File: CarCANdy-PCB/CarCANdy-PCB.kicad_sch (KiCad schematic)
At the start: 87 parts, among them J1 8P8C_Shielded, J10 ADC1, J11 ADC1, J12 ADC1, J13 Conn_01x02_Pin, J14 Conn_01x02_Pin, J15 Conn_01x02_Pin, J2 Power, J4 AUART1, J5 JSTVH3, J6 JSTVH3, J7 JSTVH3, J8 AUART1, K3 IM02, K4 IM02, K5 IM02, Q1 AO3400A, Q2 AO3400A, Q3 AO3400A, SW2 JS202011CQN, SW3 JS202011CQN, SW4 JS202011CQN, U1 LTV-357T, U2 ESP32-C3_SUPERMINI_TH, U3 SN65HVD233DR, U4 SN65HVD233DR, U5 SN65HVD233DR, U6 Teensy4.1, U7 LTV-357T, U8 LTV-357T

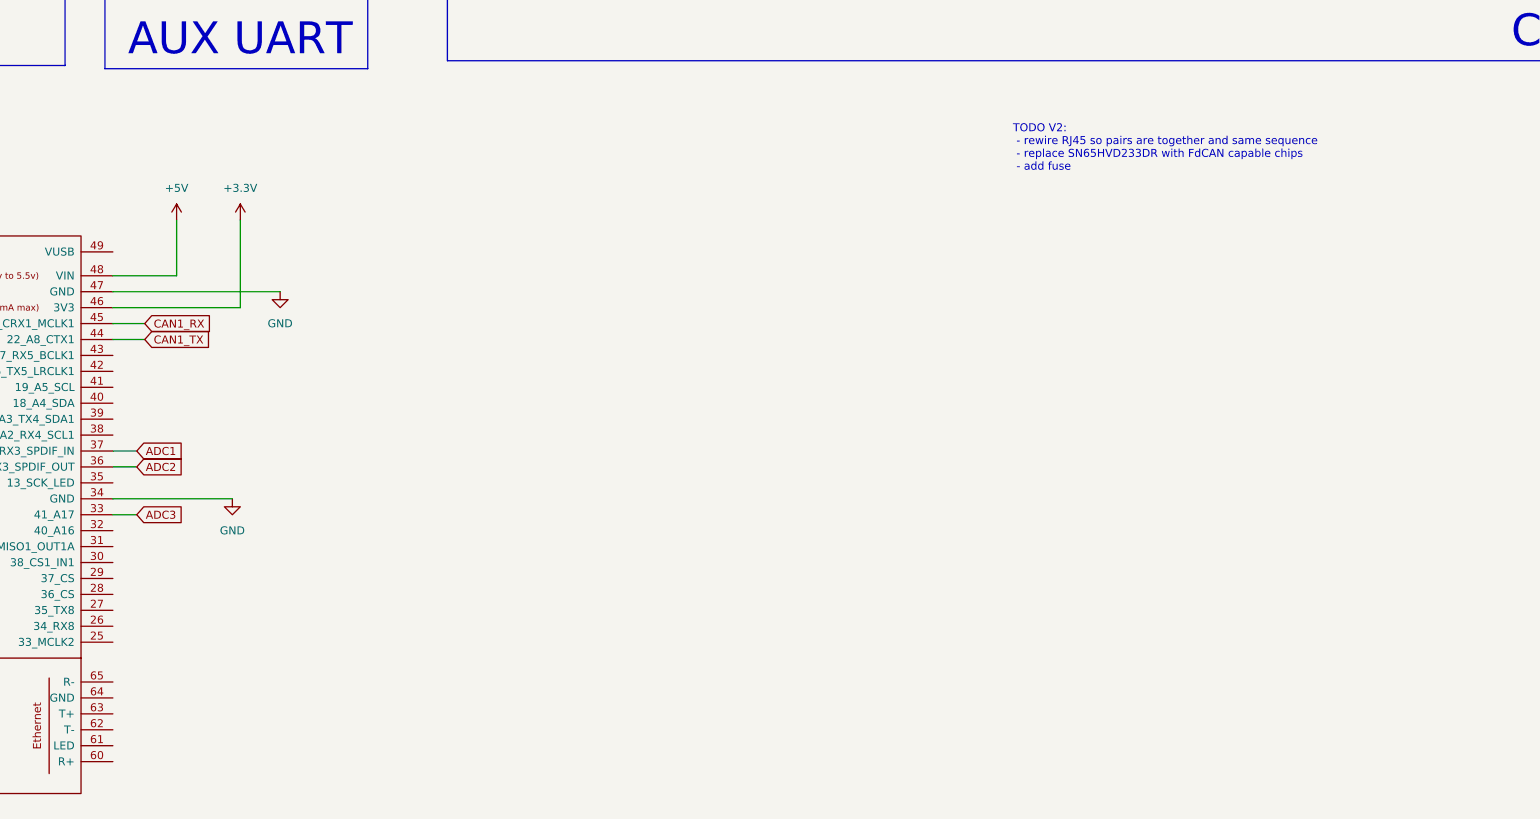
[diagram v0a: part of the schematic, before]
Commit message: simplified CANDB json
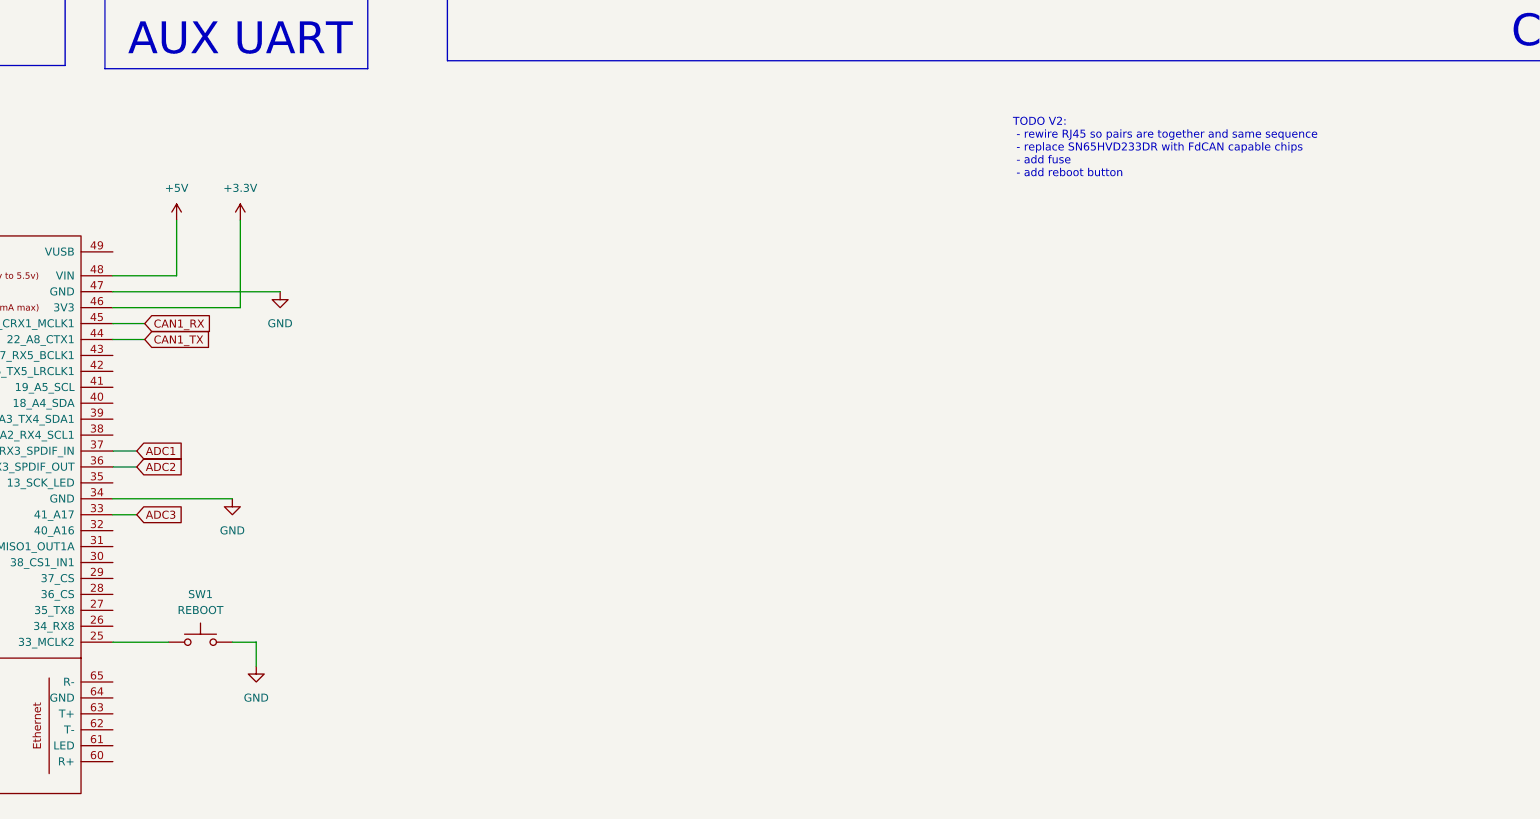
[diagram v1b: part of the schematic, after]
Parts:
- added SW1: REBOOT, Button_Switch_SMD:SW_Push_1P1T_NO_CK_KMR2, symbol Switch:SW_Push
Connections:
- net GND: now also SW1.2
- net at U6.25 (33_MCLK2): now also SW1.1
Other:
- note added: "TODO V2: - rewire RJ45 so pairs are together and same sequence - replace SN65HVD233DR with FdCAN capable chips - add fuse - add reboot button"
- note removed: "TODO V2: - rewire RJ45 so pairs are together and same sequence - replace SN65HVD233DR with FdCAN capable chips - add fuse"
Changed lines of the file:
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@@
 		)
 	)
-	(text "TODO V2: \n - rewire RJ45 so pairs are together and same sequence\n - replace SN65HVD233DR with FdCAN capable chips\n - add fuse"
+	(text "TODO V2: \n - rewire RJ45 so pairs are together and same sequence\n - replace SN65HVD233DR with FdCAN capable chips\n - add fuse\n - add reboot button"
 		(exclude_from_sim no)
 		(at 547.37 163.83 0)
@@
 	(wire
 		(pts
+			(xy 422.91 242.57) (xy 426.72 242.57)
+		)
+		(stroke
+			(width 0)
+			(type default)
+		)
+	)
+	(wire
+		(pts
 			(xy 139.7 214.63) (xy 139.7 207.01)
 		)
@@
 	(wire
 		(pts
+			(xy 403.86 242.57) (xy 412.75 242.57)
+		)
+		(stroke
+			(width 0)
+			(type default)
+		)
+	)
+	(wire
+		(pts
 			(xy 594.36 53.34) (xy 596.9 53.34)
 		)
@@
 	(wire
 		(pts
+			(xy 426.72 242.57) (xy 426.72 246.38)
+		)
+		(stroke
+			(width 0)
+			(type default)
+		)
+	)
+	(wire
+		(pts
 			(xy 344.17 189.23) (xy 347.98 189.23)
 		)
@@
 	(symbol
 		(lib_id "power:GND")
+		(at 426.72 246.38 0)
+		(unit 1)
+		(body_style 1)
+		(exclude_from_sim no)
+		(in_bom yes)
+		(on_board yes)
+		(in_pos_files yes)
+		(dnp no)
+		(fields_autoplaced yes)
+		(property "Reference" "#PWR075"
+			(at 426.72 252.73 0)
+			(hide yes)
+			(show_name no)
+			(do_not_autoplace no)
+			(effects
+				(font
+					(size 1.27 1.27)
+				)
+			)
+		)
+		(property "Value" "GND"
+			(at 426.72 251.46 0)
+			(show_name no)
+			(do_not_autoplace no)
+			(effects
+				(font
+					(size 1.27 1.27)
+				)
+			)
+		)
+		(property "Footprint" ""
+			(at 426.72 246.38 0)
+			(hide yes)
+			(show_name no)
+			(do_not_autoplace no)
+			(effects
+				(font
+					(size 1.27 1.27)
+				)
+			)
+		)
+		(property "Datasheet" ""
+			(at 426.72 246.38 0)
+			(hide yes)
+			(show_name no)
+			(do_not_autoplace no)
+			(effects
+				(font
+					(size 1.27 1.27)
+				)
+			)
+		)
+		(property "Description" "Power symbol creates a global label with name \"GND\" , ground"
+			(at 426.72 246.38 0)
+			(hide yes)
+			(show_name no)
+			(do_not_autoplace no)
+			(effects
+				(font
+					(size 1.27 1.27)
+				)
+			)
+		)
+		(pin "1"
+		)
+		(instances
+			(project "CarCANdy-PCB"
+				(path "/971987f6-db6c-4f58-a887-69a69687dd52"
+					(reference "#PWR075")
+					(unit 1)
+				)
+			)
+		)
+	)
+	(symbol
+		(lib_id "power:GND")
 		(at 50.8 151.13 0)
 		(unit 1)
@@
 					(unit 1)
 				)
+			)
+		)
+	)
+	(symbol
+		(lib_id "Switch:SW_Push")
+		(at 417.83 242.57 0)
+		(unit 1)
+		(body_style 1)
+		(exclude_from_sim no)
+		(in_bom yes)
+		(on_board yes)
+		(in_pos_files yes)
+		(dnp no)
+		(fields_autoplaced yes)
+		(property "Reference" "SW1"
+			(at 417.83 234.95 0)
+			(show_name no)
+			(do_not_autoplace no)
+			(effects
+				(font
+					(size 1.27 1.27)
+				)
+			)
+		)
+		(property "Value" "REBOOT"
+			(at 417.83 237.49 0)
+			(show_name no)
+			(do_not_autoplace no)
+			(effects
+				(font
+					(size 1.27 1.27)
+				)
+			)
+		)
+		(property "Footprint" "Button_Switch_SMD:SW_Push_1P1T_NO_CK_KMR2"
+			(at 417.83 237.49 0)
+			(hide yes)
+			(show_name no)
+			(do_not_autoplace no)
+			(effects
+				(font
+					(size 1.27 1.27)
+				)
+			)
+		)
+		(property "Datasheet" ""
+			(at 417.83 237.49 0)
+			(hide yes)
+			(show_name no)
+			(do_not_autoplace no)
+			(effects
+				(font
+					(size 1.27 1.27)
+				)
+			)
+		)
+		(property "Description" "Push button switch, generic, two pins"
+			(at 417.83 242.57 0)
+			(hide yes)
+			(show_name no)
+			(do_not_autoplace no)
+			(effects
+				(font
+					(size 1.27 1.27)
+				)
+			)
+		)
+		(pin "2"
+		)
+		(pin "1"
+		)
+		(instances
+			(project "CarCANdy-PCB"
+				(path "/971987f6-db6c-4f58-a887-69a69687dd52"
+					(reference "SW1")
+					(unit 1)
+				)

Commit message: bug fixes in PCB
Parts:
- added D15, D16: 1N4148W, Diode_SMD:D_SOD-123, symbol Diode:1N4148W
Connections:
- net +5V: now also D15.2 (A), D16.2 (A); no longer U2.5V, U6.48 (VIN)
- net CAN2_RX: now also U6.2 (0_RX1_CRX2_CS1); no longer U6.3 (1_TX1_CTX2_MISO1)
- net CAN2_TX: now also U6.3 (1_TX1_CTX2_MISO1); no longer U6.2 (0_RX1_CRX2_CS1)
- new net: D15.1 (K), U6.48 (VIN)
- new net: D16.1 (K), U2.5V
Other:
- note added: "Teensy 4.1"
- moved on the sheet: C2, C3, C4, C5, C6, C7, D10, D11, D12, D13, D14, D5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

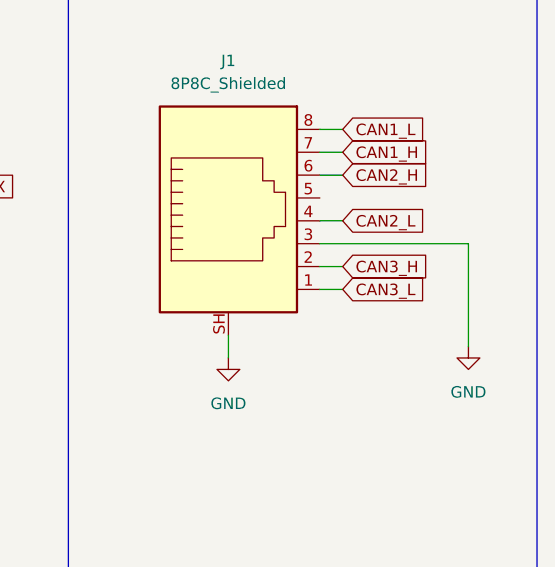
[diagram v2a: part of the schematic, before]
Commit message: added diodes to power rails, rewired RJ45
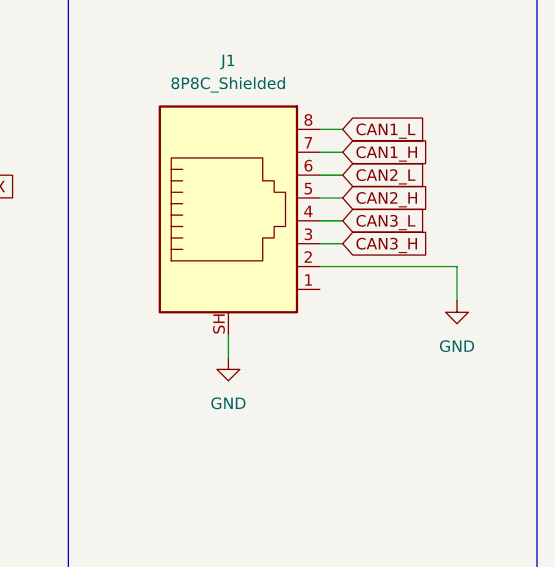
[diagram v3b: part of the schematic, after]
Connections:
- net CAN2_H: now also J1.5; no longer J1.6
- net CAN2_L: now also J1.6; no longer J1.4
- net CAN3_H: now also J1.3; no longer J1.2
- net CAN3_L: now also J1.4; no longer J1.1
- net GND: now also J1.2; no longer J1.3
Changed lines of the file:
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@@
 	(wire
 		(pts
-			(xy 796.29 67.31) (xy 798.83 67.31)
-		)
-		(stroke
-			(width 0)
-			(type default)
-		)
-	)
-	(wire
-		(pts
 			(xy 492.76 66.04) (xy 492.76 68.58)
 		)
@@
 	(wire
 		(pts
-			(xy 796.29 80.01) (xy 798.83 80.01)
-		)
-		(stroke
-			(width 0)
-			(type default)
-		)
-	)
-	(wire
-		(pts
 			(xy 612.14 290.83) (xy 613.41 290.83)
 		)
@@
 	(wire
 		(pts
-			(xy 796.29 77.47) (xy 812.8 77.47)
-		)
-		(stroke
-			(width 0)
-			(type default)
-		)
-	)
-	(wire
-		(pts
 			(xy 631.19 288.29) (xy 631.19 290.83)
 		)
@@
 	(wire
 		(pts
-			(xy 796.29 74.93) (xy 798.83 74.93)
-		)
-		(stroke
-			(width 0)
-			(type default)
-		)
-	)
-	(wire
-		(pts
 			(xy 506.73 270.51) (xy 511.81 270.51)
 		)
@@
 	(wire
 		(pts
-			(xy 565.15 220.98) (xy 565.15 198.12)
+			(xy 811.53 80.01) (xy 811.53 83.82)
 		)
 		(stroke
@@
 	(wire
 		(pts
-			(xy 609.6 86.36) (xy 610.87 86.36)
+			(xy 565.15 220.98) (xy 565.15 198.12)
 		)
 		(stroke
@@
 	(wire
 		(pts
-			(xy 570.23 267.97) (xy 607.06 267.97)
+			(xy 609.6 86.36) (xy 610.87 86.36)
 		)
 		(stroke
@@
 	(wire
 		(pts
-			(xy 172.72 50.8) (xy 176.53 50.8)
+			(xy 570.23 267.97) (xy 607.06 267.97)
 		)
 		(stroke
@@
 	(wire
 		(pts
-			(xy 511.81 290.83) (xy 513.08 290.83)
+			(xy 172.72 50.8) (xy 176.53 50.8)
 		)
 		(stroke
@@
 	(wire
 		(pts
-			(xy 812.8 88.9) (xy 812.8 77.47)
+			(xy 511.81 290.83) (xy 513.08 290.83)
 		)
 		(stroke
@@
 	(wire
 		(pts
+			(xy 796.29 72.39) (xy 798.83 72.39)
+		)
+		(stroke
+			(width 0)
+			(type default)
+		)
+	)
+	(wire
+		(pts
 			(xy 683.26 285.75) (xy 685.8 285.75)
 		)
@@
 	(wire
 		(pts
-			(xy 796.29 82.55) (xy 798.83 82.55)
-		)
-		(stroke
-			(width 0)
-			(type default)
-		)
-	)
-	(wire
-		(pts
-			(xy 796.29 64.77) (xy 798.83 64.77)
-		)
-		(stroke
-			(width 0)
-			(type default)
-		)
-	)
-	(wire
-		(pts
 			(xy 511.81 302.26) (xy 511.81 295.91)
 		)
@@
 	(wire
 		(pts
+			(xy 796.29 64.77) (xy 798.83 64.77)
+		)
+		(stroke
+			(width 0)
+			(type default)
+		)
+	)
+	(wire
+		(pts
 			(xy 515.62 215.9) (xy 515.62 218.44)
 		)
@@
 	(wire
 		(pts
+			(xy 796.29 77.47) (xy 798.83 77.47)
+		)
+		(stroke
+			(width 0)
+			(type default)
+		)
+	)
+	(wire
+		(pts
 			(xy 176.53 115.57) (xy 176.53 118.11)
 		)
@@
 	(wire
 		(pts
-			(xy 796.29 69.85) (xy 798.83 69.85)
-		)
-		(stroke
-			(width 0)
-			(type default)
-		)
-	)
-	(wire
-		(pts
 			(xy 699.77 53.34) (xy 706.12 53.34)
 		)
@@
 	(wire
 		(pts
+			(xy 796.29 69.85) (xy 798.83 69.85)
+		)
+		(stroke
+			(width 0)
+			(type default)
+		)
+	)
+	(wire
+		(pts
 			(xy 486.41 285.75) (xy 488.95 285.75)
 		)
@@
 	(wire
 		(pts
+			(xy 796.29 74.93) (xy 798.83 74.93)
+		)
+		(stroke
+			(width 0)
+			(type default)
+		)
+	)
+	(wire
+		(pts
 			(xy 485.14 78.74) (xy 485.14 81.28)
 		)
@@
 	(wire
 		(pts
+			(xy 796.29 80.01) (xy 811.53 80.01)
+		)
+		(stroke
+			(width 0)
+			(type default)
+		)
+	)
+	(wire
+		(pts
 			(xy 720.09 203.2) (xy 712.47 203.2)
 		)
@@
 	(wire
 		(pts
+			(xy 796.29 67.31) (xy 798.83 67.31)
+		)
+		(stroke
+			(width 0)
+			(type default)
+		)
+	)
+	(wire
+		(pts
 			(xy 172.72 81.28) (xy 176.53 81.28)
 		)
@@
 	(global_label "CAN3_H"
 		(shape input)
-		(at 798.83 80.01 0)
+		(at 798.83 77.47 0)
 		(fields_autoplaced yes)
 		(effects
@@
 		)
 		(property "Intersheetrefs" "${INTERSHEET_REFS}"
-			(at 809.0119 80.01 0)
+			(at 809.0119 77.47 0)
 			(show_name no)
 			(do_not_autoplace no)
@@
 	(global_label "CAN2_L"
 		(shape input)
-		(at 798.83 74.93 0)
+		(at 798.83 69.85 0)
 		(fields_autoplaced yes)
 		(effects
@@
 		)
 		(property "Intersheetrefs" "${INTERSHEET_REFS}"
-			(at 808.7095 74.93 0)
+			(at 808.7095 69.85 0)
 			(show_name no)
 			(do_not_autoplace no)
@@
 	(global_label "CAN2_H"
 		(shape input)
-		(at 798.83 69.85 0)
+		(at 798.83 72.39 0)
 		(fields_autoplaced yes)
 		(effects
@@
 		)
 		(property "Intersheetrefs" "${INTERSHEET_REFS}"
-			(at 809.0119 69.85 0)
+			(at 809.0119 72.39 0)
 			(show_name no)
 			(do_not_autoplace no)
@@
 	(global_label "CAN3_L"
 		(shape input)
-		(at 798.83 82.55 0)
+		(at 798.83 74.93 0)
 		(fields_autoplaced yes)
 		(effects
@@
 		)
 		(property "Intersheetrefs" "${INTERSHEET_REFS}"
-			(at 808.7095 82.55 0)
+			(at 808.7095 74.93 0)
 			(show_name no)
 			(do_not_autoplace no)
@@
 	(symbol
 		(lib_id "power:GND")
-		(at 812.8 88.9 0)
+		(at 811.53 83.82 0)
 		(unit 1)
 		(body_style 1)
@@
 		(fields_autoplaced yes)
 		(property "Reference" "#PWR027"
-			(at 812.8 95.25 0)
+			(at 811.53 90.17 0)
 			(hide yes)
 			(show_name no)
@@
 		)
 		(property "Value" "GND"
-			(at 812.8 93.98 0)
+			(at 811.53 88.9 0)
 			(show_name no)
 			(do_not_autoplace no)
@@
 		)
 		(property "Footprint" ""
-			(at 812.8 88.9 0)
+			(at 811.53 83.82 0)
 			(hide yes)
 			(show_name no)
@@
 		)
 		(property "Datasheet" ""
-			(at 812.8 88.9 0)
+			(at 811.53 83.82 0)
 			(hide yes)
 			(show_name no)
@@
 		)
 		(property "Description" "Power symbol creates a global label with name \"GND\" , ground"
-			(at 812.8 88.9 0)
+			(at 811.53 83.82 0)
 			(hide yes)
 			(show_name no)

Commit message: Update project and exclude local datasets
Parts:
- added D4, D6: NeoPixel_THT, Package_DFN_QFN:Nordic_AQFN-94-1EP_7x7mm_P0.4mm, symbol LED:NeoPixel_THT
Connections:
- net +5V: now also D4.3 (VDD), D6.3 (VDD)
- net GND: now also D4.2 (GND), D6.2 (GND)
- net NEOLED: now reaches U6.39 (17_A3_TX4_SDA1)
- net NEOLED: now also D4.4 (DIN)
- new net: D4.1 (DOUT), D6.4 (DIN)
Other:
- note added: "CAN3"
- note added: "TODO V2: - rewire RJ45 so pairs are together and same sequence - replace SN65HVD233DR with FdCAN capable chips - add fuse - add reboot button - add buzzer - add 2xneopixels"
- note removed: "TODO V2: - rewire RJ45 so pairs are together and same sequence - replace SN65HVD233DR with FdCAN capable chips - add fuse - add reboot button"
